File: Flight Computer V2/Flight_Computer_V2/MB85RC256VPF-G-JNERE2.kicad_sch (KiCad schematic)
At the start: 7 parts, among them IC1 MB85RC256VPF-G-JNERE2

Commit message: finalized schematic, added datasheets, and pdf of schematic
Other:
- company: (none) -> By: Dylan Haussecker
- title: (none) -> Avionics Flight Computer
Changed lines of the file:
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@@
 (kicad_sch (version 20230121) (generator eeschema)
   (paper "A4")
+  (title_block
+    (title "Avionics Flight Computer")
+    (date "2023-09-04")
+    (rev "1.0")
+    (company "By: Dylan Haussecker")
+  )
   (junction (at 187.96 77.47) (diameter 0) (color 0 0 0 0)
   )

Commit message: updated pcb
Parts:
- removed R14: 10k, symbol Device:R_Small
- added R6: 10k, Resistor_SMD:R_0402_1005Metric, symbol Device:R_Small
- IC1: footprint SOIC127P798X210-8N -> LibraryLoader:SOIC127P798X210-8N
- JP3: footprint (none) -> Jumper:SolderJumper-2_P1.3mm_Open_Pad1.0x1.5mm
- R15: footprint (none) -> Resistor_SMD:R_0402_1005Metric
- TP3: footprint (none) -> TestPoint:TestPoint_Pad_D1.0mm
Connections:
- net +3V3: now also R6.1
- net at IC1.6 (SCL), JP3.1 (A), TP3.1: now also R6.2
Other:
- moved on the sheet: JP3, TP3

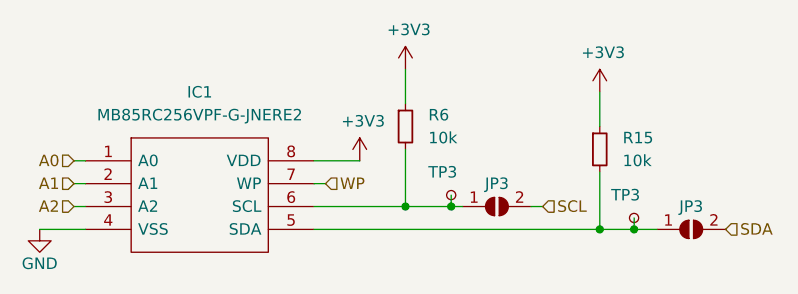
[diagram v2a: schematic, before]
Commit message: changed new flight computer scl resistors
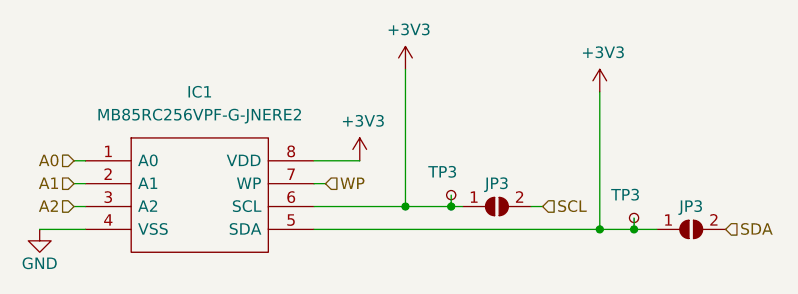
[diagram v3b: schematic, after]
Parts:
- removed R15, R6: 10k, Resistor_SMD:R_0402_1005Metric, symbol Device:R_Small
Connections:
- net +3V3: now also IC1.5 (SDA), IC1.6 (SCL), JP3.1 (A), JP3.1 (A), TP3.1, TP3.1
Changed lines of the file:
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@@
     (stroke (width 0) (type default))
   )
-  (wire (pts (xy 162.56 59.69) (xy 162.56 63.5))
+  (wire (pts (xy 162.56 59.69) (xy 162.56 74.93))
     (stroke (width 0) (type default))
   )
@@
     (stroke (width 0) (type default))
   )
-  (wire (pts (xy 162.56 68.58) (xy 162.56 74.93))
-    (stroke (width 0) (type default))
-  )
   (wire (pts (xy 121.92 77.47) (xy 127 77.47))
     (stroke (width 0) (type default))
@@
     (stroke (width 0) (type default))
   )
-  (wire (pts (xy 184.15 62.23) (xy 184.15 66.04))
-    (stroke (width 0) (type default))
-  )
   (wire (pts (xy 152.4 74.93) (xy 162.56 74.93))
     (stroke (width 0) (type default))
@@
     (stroke (width 0) (type default))
   )
-  (wire (pts (xy 184.15 71.12) (xy 184.15 77.47))
+  (wire (pts (xy 184.15 62.23) (xy 184.15 77.47))
     (stroke (width 0) (type default))
   )
@@
     )
   )
-  (symbol (lib_id "Device:R_Small") (at 162.56 66.04 0) (unit 1)
-    (in_bom yes) (on_board yes) (dnp no) (fields_autoplaced)
-    (property "Reference" "R6" (at 165.1 64.77 0)
-      (effects (font (size 1.27 1.27)) (justify left))
-    )
-    (property "Value" "10k" (at 165.1 67.31 0)
-      (effects (font (size 1.27 1.27)) (justify left))
-    )
-    (property "Footprint" "Resistor_SMD:R_0402_1005Metric" (at 162.56 66.04 0)
-      (effects (font (size 1.27 1.27)) hide)
-    )
-    (property "Datasheet" "~" (at 162.56 66.04 0)
-      (effects (font (size 1.27 1.27)) hide)
-    )
-    (pin "1")
-    (pin "2")
-    (instances
-      (project "Flight_Computer_V2"
-        (path "/39d7ebb3-b69d-4ae9-8f55-c9acfe77d345/728ff691-86aa-4406-a714-359017417c15"
-          (reference "R6") (unit 1)
-        )
-        (path "/39d7ebb3-b69d-4ae9-8f55-c9acfe77d345/de413d1f-8d39-42d8-b833-6419d9c73587"
-          (reference "R7") (unit 1)
-        )
-        (path "/39d7ebb3-b69d-4ae9-8f55-c9acfe77d345/806e3fbd-cca2-40cb-b727-86767e32e959"
-          (reference "R14") (unit 1)
-        )
-        (path "/39d7ebb3-b69d-4ae9-8f55-c9acfe77d345/5302a5ff-4c5a-40f5-8b82-1f5be512d366"
-          (reference "R16") (unit 1)
-        )
-      )
-    )
-  )
   (symbol (lib_id "power:GND") (at 121.92 77.47 0) (unit 1)
     (in_bom yes) (on_board yes) (dnp no)
@@
         )
       )
-    )
-  )
-  (symbol (lib_id "Device:R_Small") (at 184.15 68.58 0) (unit 1)
-    (in_bom yes) (on_board yes) (dnp no) (fields_autoplaced)
-    (property "Reference" "R15" (at 186.69 67.31 0)
-      (effects (font (size 1.27 1.27)) (justify left))
-    )
-    (property "Value" "10k" (at 186.69 69.85 0)
-      (effects (font (size 1.27 1.27)) (justify left))
-    )
-    (property "Footprint" "Resistor_SMD:R_0402_1005Metric" (at 184.15 68.58 0)
-      (effects (font (size 1.27 1.27)) hide)
-    )
-    (property "Datasheet" "~" (at 184.15 68.58 0)
-      (effects (font (size 1.27 1.27)) hide)
-    )
-    (pin "1")
-    (pin "2")
-    (instances
-      (project "Flight_Computer_V2"
-        (path "/39d7ebb3-b69d-4ae9-8f55-c9acfe77d345/728ff691-86aa-4406-a714-359017417c15"
-          (reference "R15") (unit 1)
-        )
-        (path "/39d7ebb3-b69d-4ae9-8f55-c9acfe77d345/de413d1f-8d39-42d8-b833-6419d9c73587"
-          (reference "R17") (unit 1)
-        )
-        (path "/39d7ebb3-b69d-4ae9-8f55-c9acfe77d345/806e3fbd-cca2-40cb-b727-86767e32e959"
-          (reference "R19") (unit 1)
-        )
-        (path "/39d7ebb3-b69d-4ae9-8f55-c9acfe77d345/5302a5ff-4c5a-40f5-8b82-1f5be512d366"
-          (reference "R21") (unit 1)
-        )
-      )
